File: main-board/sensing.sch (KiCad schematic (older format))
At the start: 24 parts

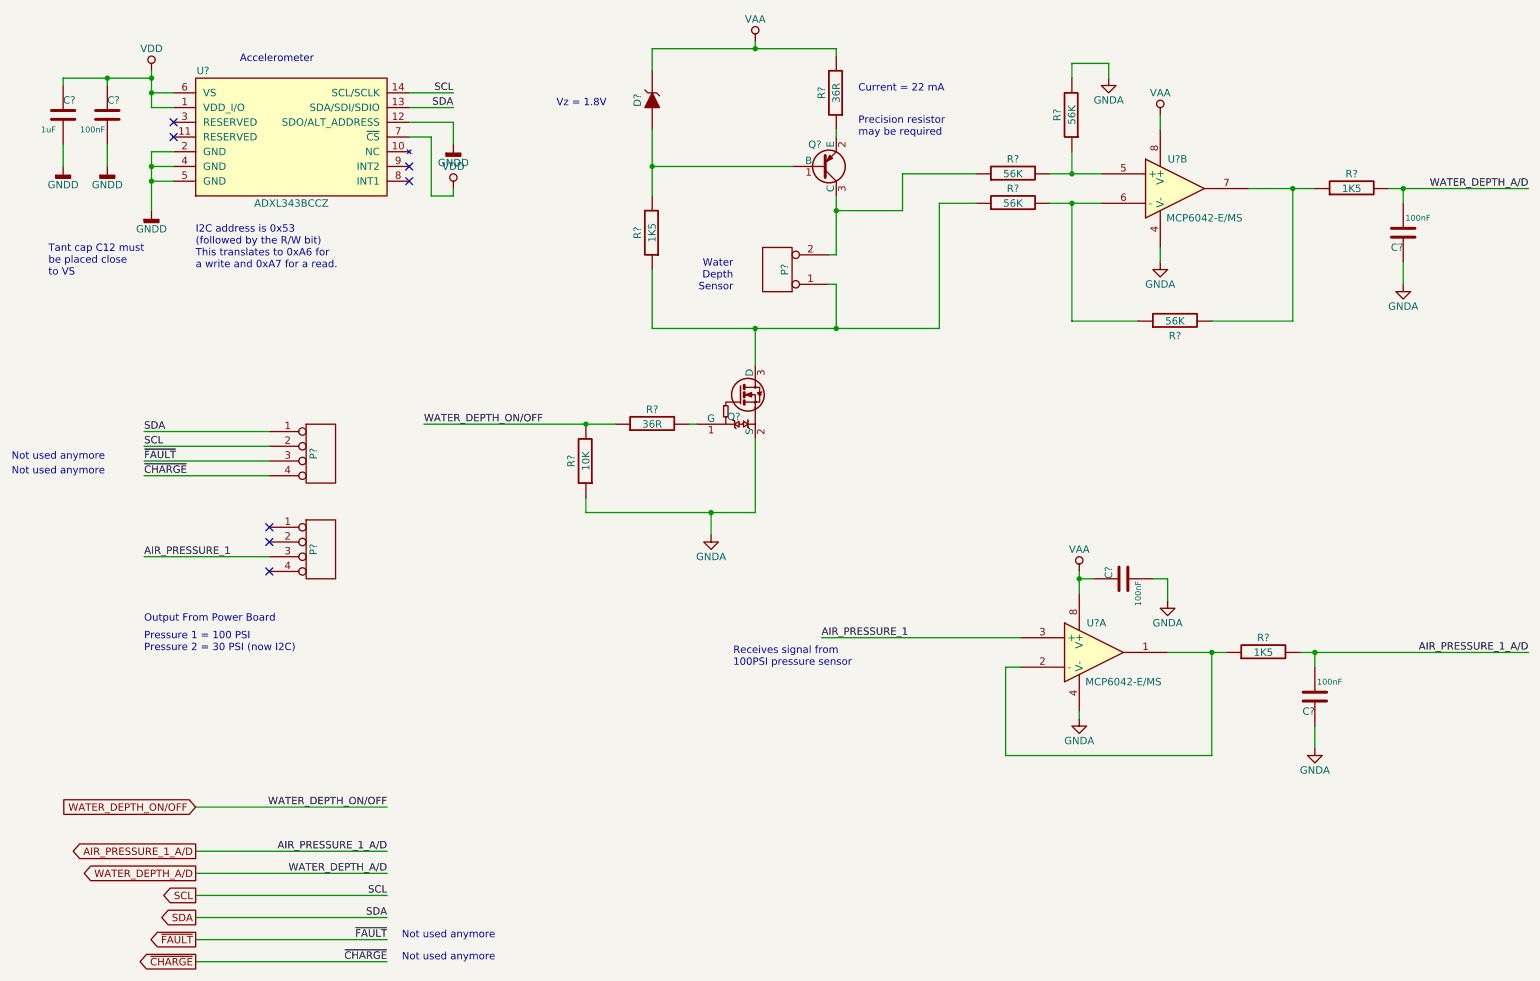
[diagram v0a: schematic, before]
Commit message: Added output files, gerbers, dril files, raster images, and updates to PCB design files.
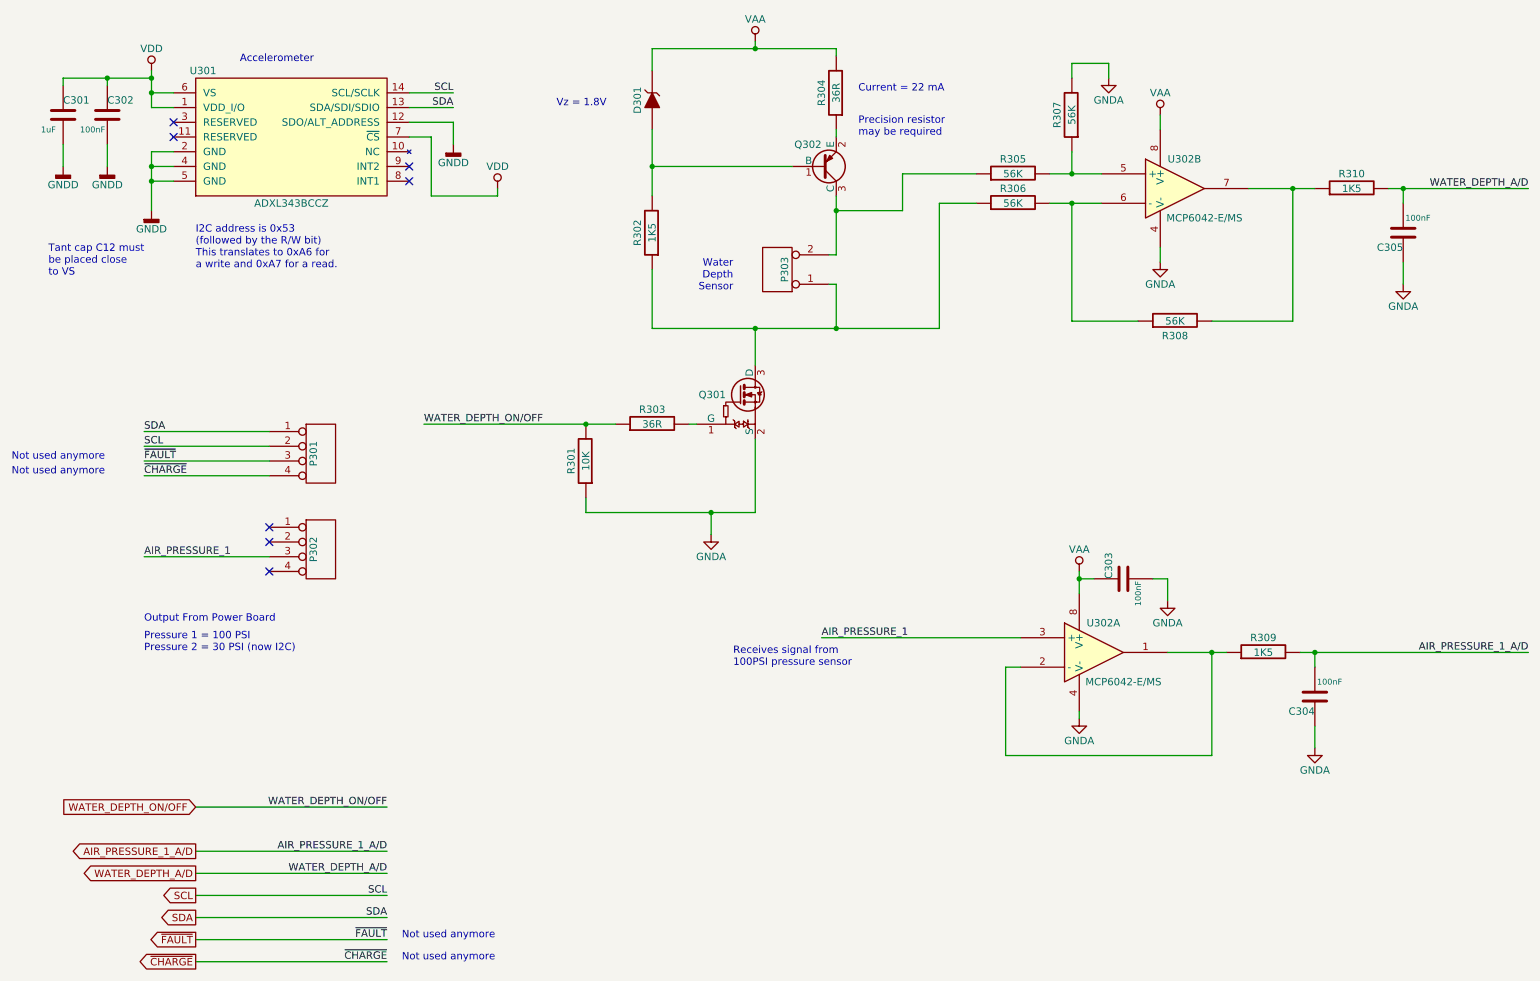
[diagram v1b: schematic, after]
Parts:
- gave numbers to parts that had none: 23
